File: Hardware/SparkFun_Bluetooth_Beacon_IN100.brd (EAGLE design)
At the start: 25.4 x 25.4 mm, 62 parts, among them J3 Vertical Qwiic Connector, U1 IN100, Y1 CRYSTAL-26MHZSMD-3.2X2.5

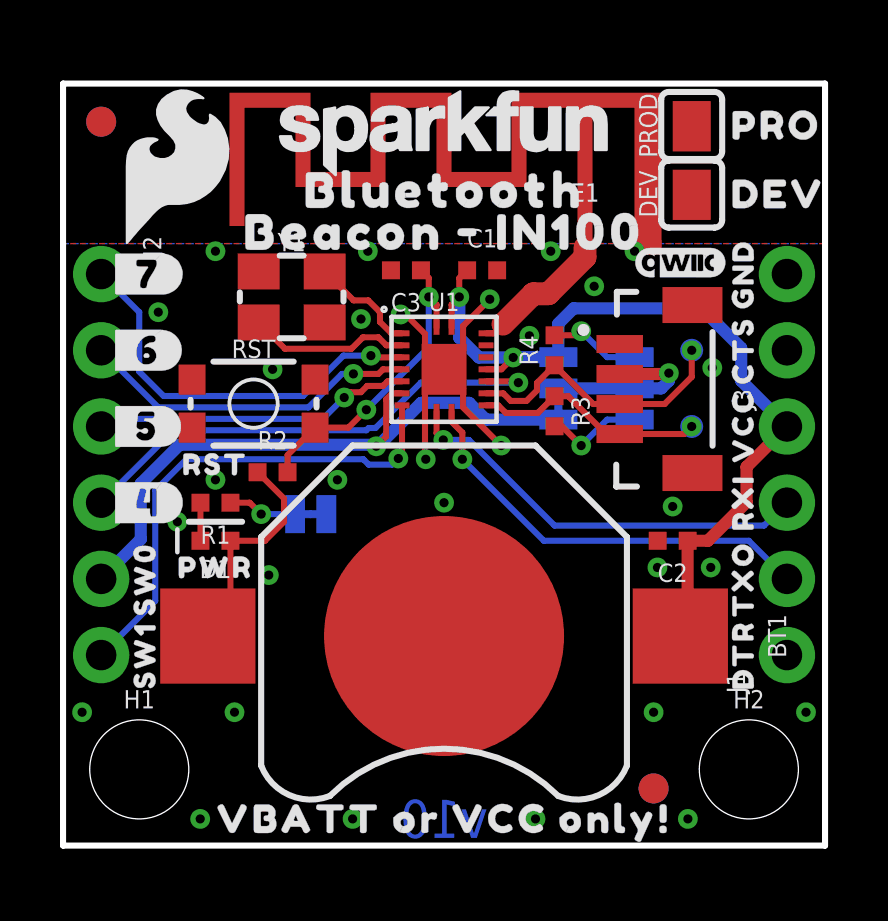
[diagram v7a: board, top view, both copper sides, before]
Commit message: Add EN test point
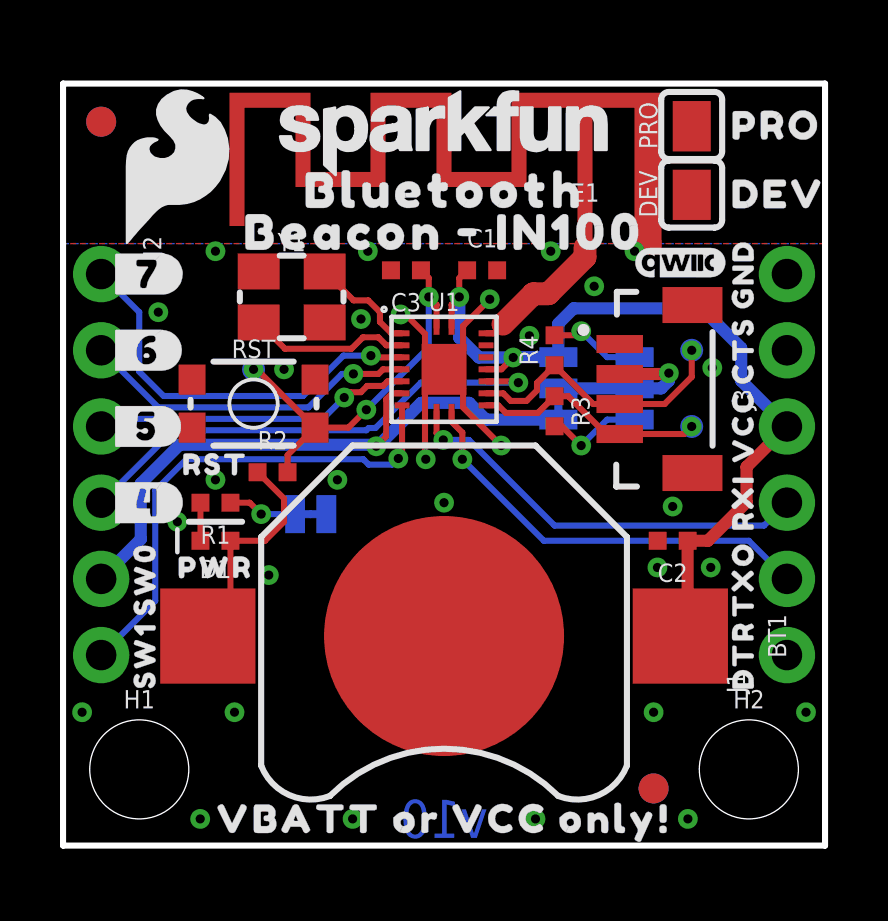
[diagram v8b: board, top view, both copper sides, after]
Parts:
- added TP3: TEST-POINT3, SparkFun-Connectors:PAD.03X.03
- renumbered PROD to PRO
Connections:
- net EN: now also TP3.1
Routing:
- net EN: track 10.6 -> 13.4 mm, vias 2 -> 3
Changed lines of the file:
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@@
 <element name="LOGO3" library="SparkFun-Aesthetics" package="QWIIC_3MM" value="QWIIC_LOGO_3MM" x="20.574" y="19.431" smashed="yes"/>
 <element name="U$28" library="output" package="DEV0" value="" x="21.59" y="21.717" smashed="yes"/>
-<element name="PROD" library="SparkFun-Aesthetics" package="PRODUCT_IDENT_PASTE_SILK" value="PROD_ID_PASTE_SILK" x="20.955" y="24.003" smashed="yes" rot="R90">
+<element name="PRO" library="SparkFun-Aesthetics" package="PRODUCT_IDENT_PASTE_SILK" value="PROD_ID_PASTE_SILK" x="20.955" y="24.003" smashed="yes" rot="R90">
 <attribute name="NAME" x="19.812" y="24.003" size="0.6096" layer="25" font="vector" ratio="20" rot="R90" align="bottom-center"/>
 <attribute name="VALUE" x="22.098" y="24.003" size="0.6096" layer="27" font="vector" ratio="20" rot="R90" align="top-center"/>
@@
 </element>
 <element name="U$30" library="output" package="PRO0" value="" x="21.59" y="24.003" smashed="yes"/>
+<element name="TP3" library="SparkFun-Connectors" package="PAD.03X.03" value="TEST-POINT3" x="6.35" y="15.875" smashed="yes" rot="MR0"/>
 </elements>
 <signals>
@@
 <contactref element="RST" pad="3"/>
 <via x="9.9314" y="17.5514" extent="1-16" drill="0.3048"/>
-<via x="6.985" y="15.875" extent="1-16" drill="0.3048"/>
+<via x="7.366" y="15.875" extent="1-16" drill="0.3048"/>
 <via x="5.08" y="12.192" extent="1-16" drill="0.3048"/>
 <via x="3.81" y="10.795" extent="1-16" drill="0.3048"/>
@@
 <wire x1="7.485" y1="12.446" x2="7.485" y2="13.017" width="0.2032" layer="1"/>
 <wire x1="7.485" y1="13.017" x2="8.4" y2="13.932" width="0.2032" layer="1"/>
-<wire x1="7.485" y1="12.446" x2="4.3" y2="13.932" width="0" layer="19" extent="1-1"/>
+<contactref element="TP3" pad="1"/>
+<via x="6.35" y="15.875" extent="1-16" drill="0.3048"/>
+<wire x1="8.4" y1="13.932" x2="6.457" y2="15.875" width="0.2032" layer="1"/>
+<wire x1="6.457" y1="15.875" x2="6.35" y2="15.875" width="0.2032" layer="1"/>
+<wire x1="6.35" y1="15.875" x2="4.3" y2="13.932" width="0" layer="19" extent="1-16"/>
 </signal>
 <signal name="N$3">
